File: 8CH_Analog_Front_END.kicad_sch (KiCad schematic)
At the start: 0 parts

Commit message: Routing the Digital Part
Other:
- sheet AFE_BLOCK1 renamed AFE_BLOCK_0
- sheet RFSoC_Connector_X1 ports: added B84.L1N_D01_AW5, B84.L1P_D00_AW6, B84.L2N_D03_AW3, B84.L2P_D02_AW4, B84.L3N_D05_AV2, B84.L3P_D04_AV3, B84.L4P_D06_AU2, B84.L5N_D09_AV5, B84.L5P_D08_AV6, B84.L6N_D11_AU3, B84.L6P_D10_AU4; removed none
- note added: "MUX Toggle Pin Out MUX Addr S0 Pin Out MUX Addr S1 Pin Out MUX Addr S2 Pin Out"
- note added: "RF_Swtich_Control_Pin_CH_0_CH1 RF_Swtich_Control_Pin_CH_2_CH3 RF_Swtich_Control_Pin_CH_4_CH5 RF_Swtich_Control_Pin_CH_6_CH7"
- note added: "Serial DATA Serial CLOCK Serial D_LATCH"

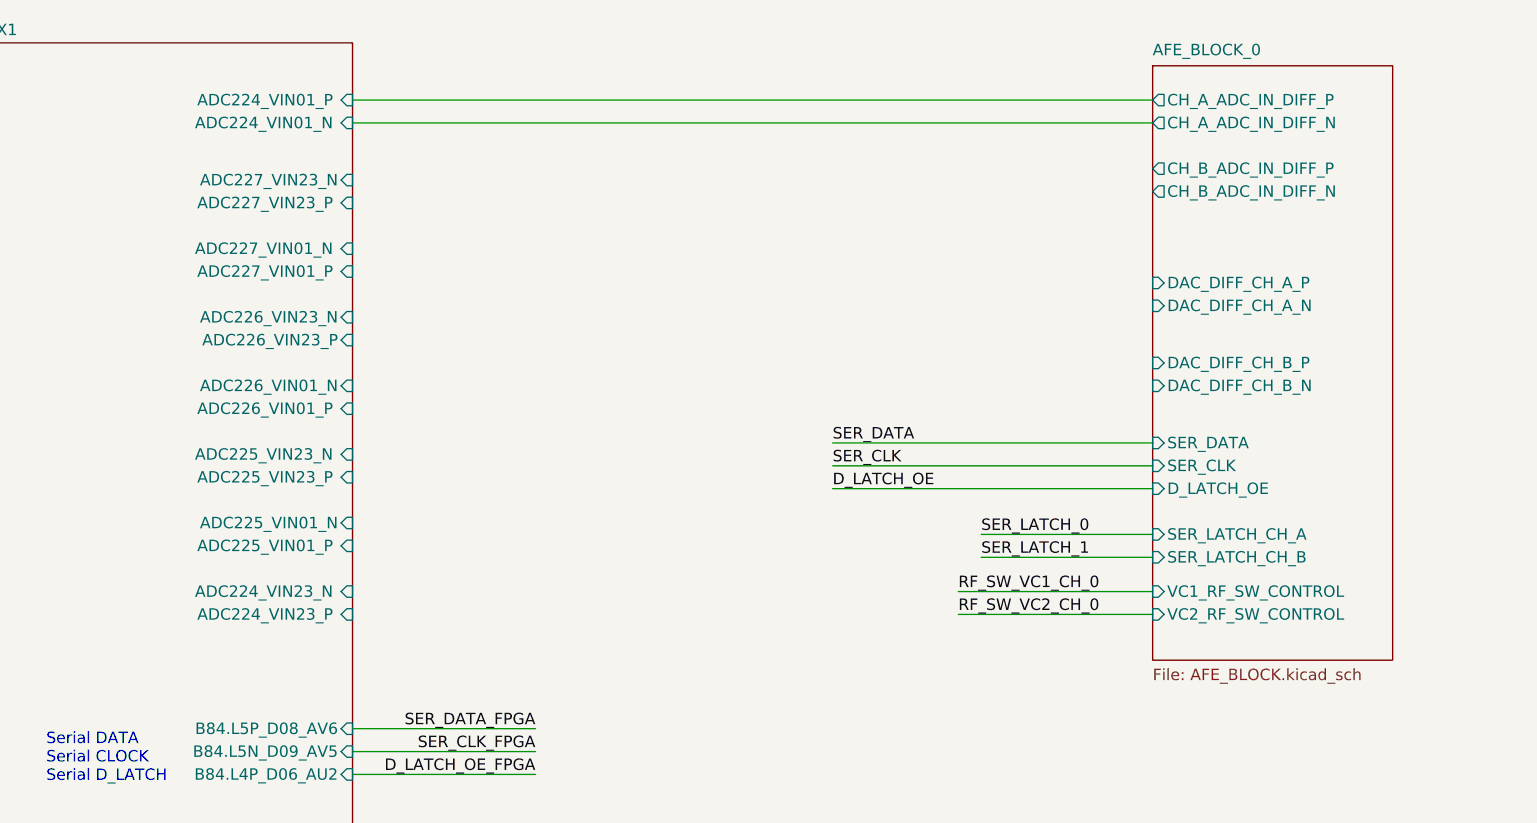
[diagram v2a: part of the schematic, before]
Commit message: Routing the Power Sector
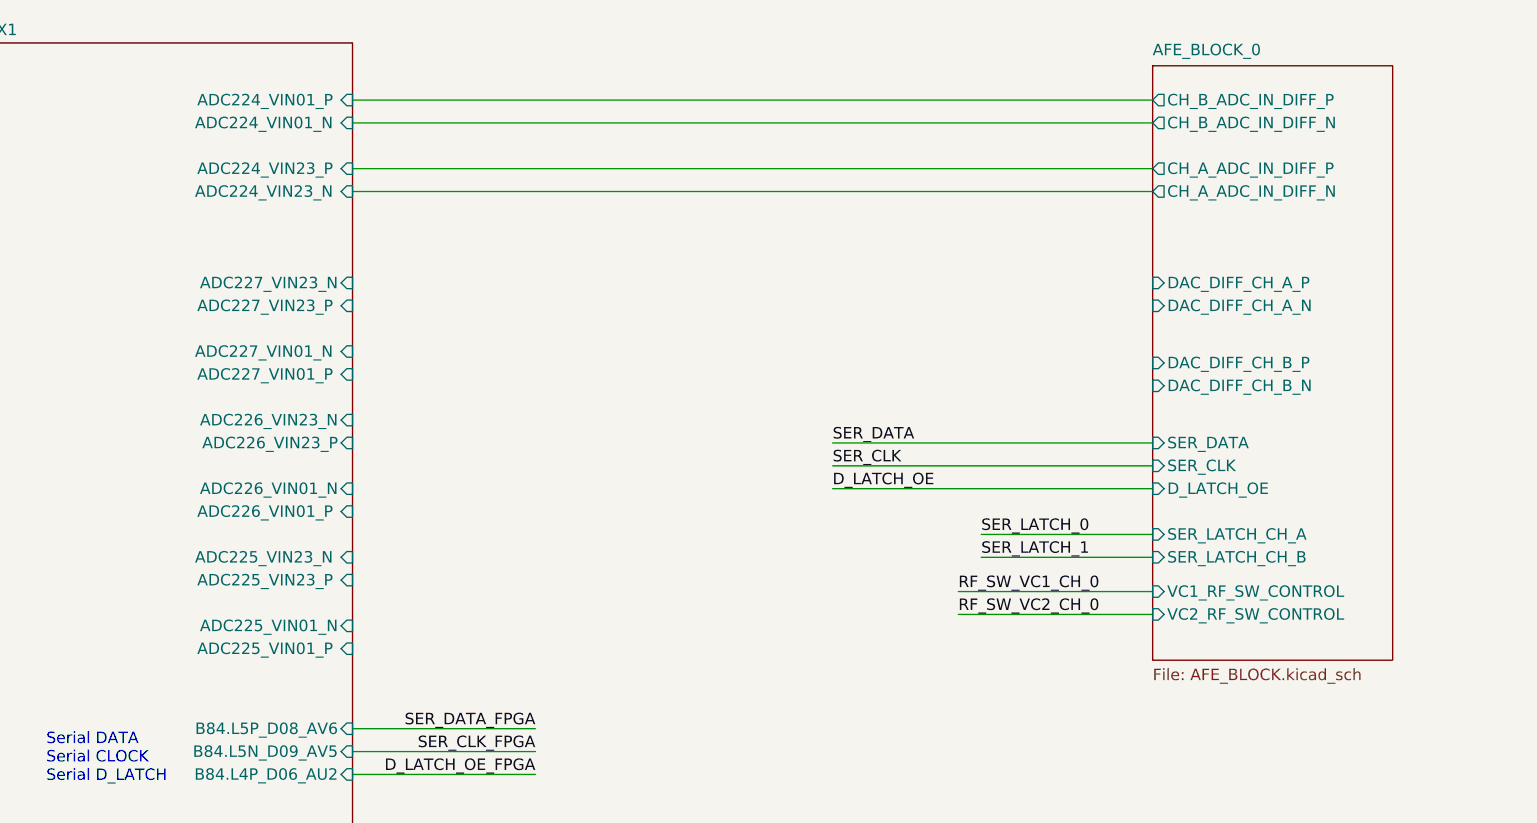
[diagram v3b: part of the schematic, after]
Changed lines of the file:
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@@
+	(wire
+		(pts
+			(xy 101.6 31.75) (xy 190.5 31.75)
+		)
+		(stroke
+			(width 0)
+			(type default)
+		)
+	)
 	(wire
 		(pts
@@
 	(wire
 		(pts
+			(xy 101.6 34.29) (xy 190.5 34.29)
+		)
+		(stroke
+			(width 0)
+			(type default)
+		)
+	)
+	(wire
+		(pts
 			(xy 149.86 124.46) (xy 170.18 124.46)
 		)
@@
 	(wire
 		(pts
-			(xy 101.6 34.29) (xy 190.5 34.29)
-		)
-		(stroke
-			(width 0)
-			(type default)
-		)
-	)
-	(wire
-		(pts
 			(xy 125.73 124.46) (xy 101.6 124.46)
 		)
@@
 	(wire
 		(pts
+			(xy 101.6 41.91) (xy 190.5 41.91)
+		)
+		(stroke
+			(width 0)
+			(type default)
+		)
+	)
+	(wire
+		(pts
 			(xy 149.86 121.92) (xy 170.18 121.92)
 		)
@@
 	(wire
 		(pts
+			(xy 101.6 39.37) (xy 190.5 39.37)
+		)
+		(stroke
+			(width 0)
+			(type default)
+		)
+	)
+	(wire
+		(pts
 			(xy 190.5 86.36) (xy 168.91 86.36)
 		)
@@
 		(pts
 			(xy 118.11 139.7) (xy 101.6 139.7)
-		)
-		(stroke
-			(width 0)
-			(type default)
-		)
-	)
-	(wire
-		(pts
-			(xy 101.6 31.75) (xy 190.5 31.75)
 		)
 		(stroke
@@
 		)
 		(pin "ADC227_VIN01_N " input
-			(at 101.6 48.26 0)
+			(at 101.6 59.69 0)
 			(effects
 				(font
@@
 		)
 		(pin "ADC227_VIN23_N" input
-			(at 101.6 40.64 0)
+			(at 101.6 52.07 0)
 			(effects
 				(font
@@
 		)
 		(pin "ADC225_VIN23_P " input
-			(at 101.6 73.66 0)
+			(at 101.6 85.09 0)
 			(effects
 				(font
@@
 		)
 		(pin "ADC224_VIN23_N " input
-			(at 101.6 86.36 0)
+			(at 101.6 41.91 0)
 			(effects
 				(font
@@
 		)
 		(pin "ADC224_VIN23_P " input
-			(at 101.6 88.9 0)
+			(at 101.6 39.37 0)
 			(effects
 				(font
@@
 		)
 		(pin "ADC225_VIN01_N" input
-			(at 101.6 78.74 0)
+			(at 101.6 90.17 0)
 			(effects
 				(font
@@
 		)
 		(pin "ADC225_VIN01_P " input
-			(at 101.6 81.28 0)
+			(at 101.6 92.71 0)
 			(effects
 				(font
@@
 		)
 		(pin "ADC226_VIN23_P" input
-			(at 101.6 58.42 0)
+			(at 101.6 69.85 0)
 			(effects
 				(font
@@
 		)
 		(pin "ADC226_VIN23_N" input
-			(at 101.6 55.88 0)
+			(at 101.6 67.31 0)
 			(effects
 				(font
@@
 		)
 		(pin "ADC227_VIN23_P " input
-			(at 101.6 43.18 0)
+			(at 101.6 54.61 0)
 			(effects
 				(font
@@
 		)
 		(pin "ADC227_VIN01_P " input
-			(at 101.6 50.8 0)
+			(at 101.6 62.23 0)
 			(effects
 				(font
@@
 		)
 		(pin "ADC226_VIN01_P " input
-			(at 101.6 66.04 0)
+			(at 101.6 77.47 0)
 			(effects
 				(font
@@
 		)
 		(pin "ADC226_VIN01_N" input
-			(at 101.6 63.5 0)
+			(at 101.6 74.93 0)
 			(effects
 				(font
@@
 		)
 		(pin "ADC225_VIN23_N " input
-			(at 101.6 71.12 0)
+			(at 101.6 82.55 0)
 			(effects
 				(font
@@
 		)
 		(pin "CH_A_ADC_IN_DIFF_N" output
-			(at 190.5 34.29 180)
+			(at 190.5 41.91 180)
 			(effects
 				(font
@@
 		)
 		(pin "CH_A_ADC_IN_DIFF_P" output
-			(at 190.5 31.75 180)
+			(at 190.5 39.37 180)
 			(effects
 				(font
@@
 		)
 		(pin "CH_B_ADC_IN_DIFF_P" output
-			(at 190.5 39.37 180)
+			(at 190.5 31.75 180)
 			(effects
 				(font
@@
 		)
 		(pin "CH_B_ADC_IN_DIFF_N" output
-			(at 190.5 41.91 180)
-			(effects
-				(font
+			(at 190.5 34.29 180)
+			(effects
+				(font

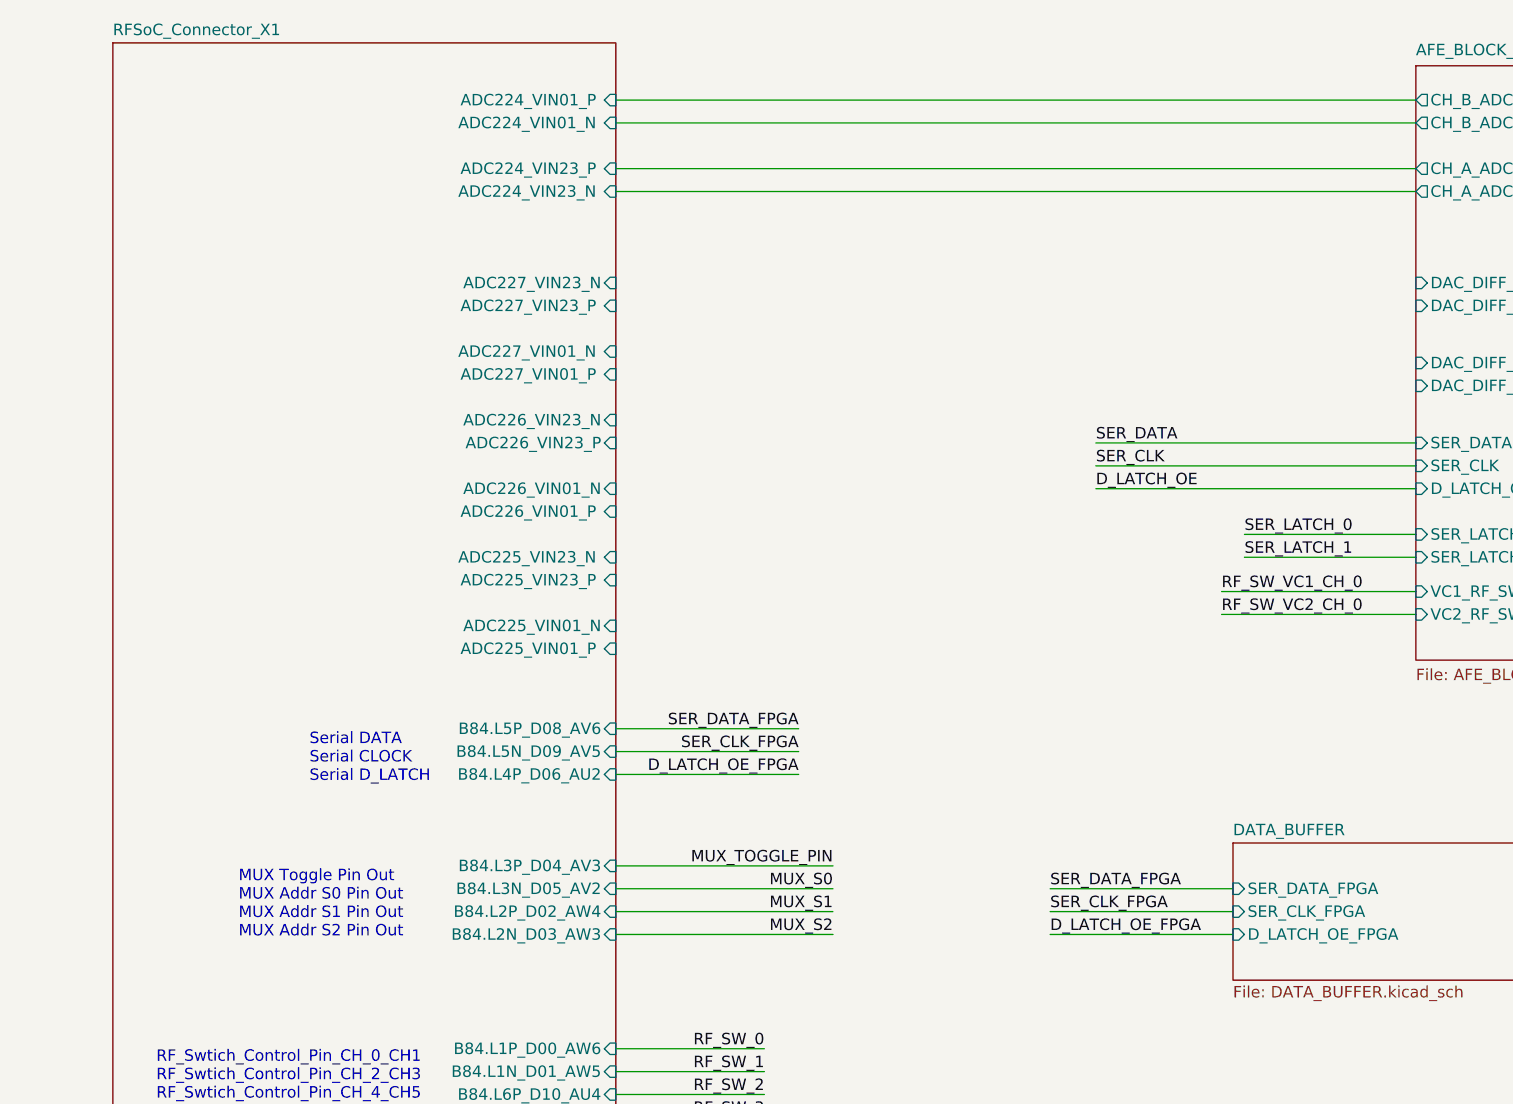
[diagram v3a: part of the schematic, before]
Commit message: Inverted the VGA output
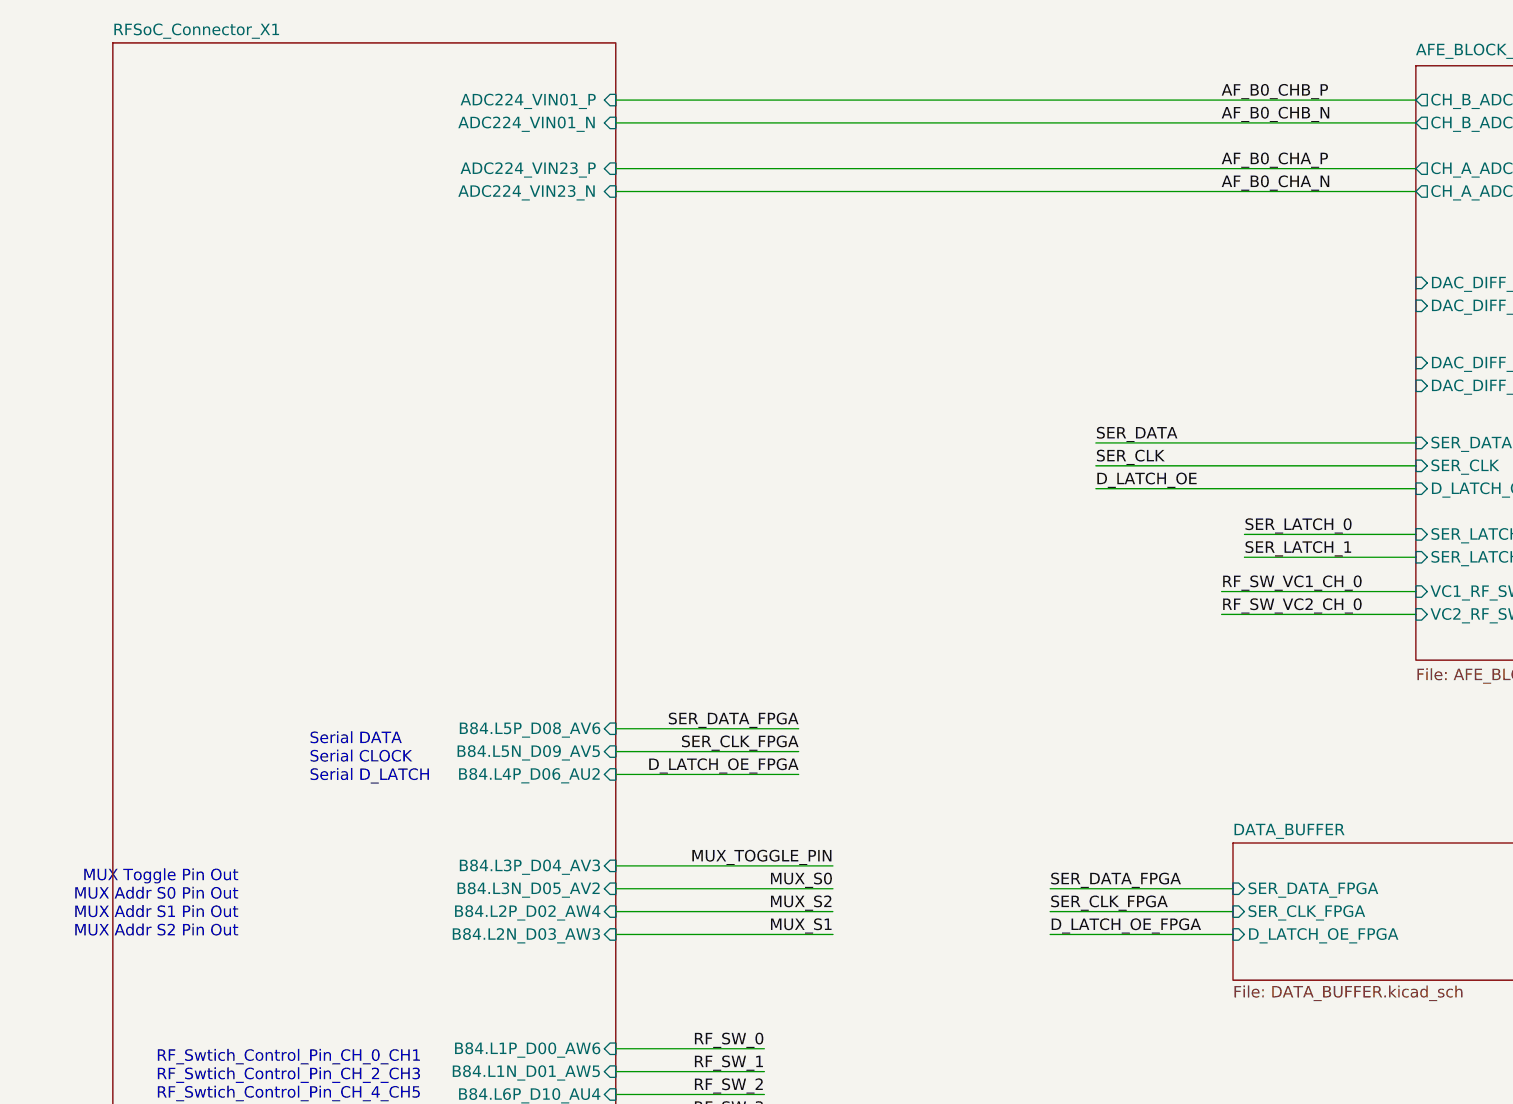
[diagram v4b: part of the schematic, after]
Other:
- sheet RFSoC_Connector_X1 ports: added none; removed ADC225_VIN01_N, ADC225_VIN01_P , ADC225_VIN23_N , ADC225_VIN23_P , ADC226_VIN01_N, ADC226_VIN01_P , ADC226_VIN23_N, ADC226_VIN23_P, ADC227_VIN01_N , ADC227_VIN01_P , ADC227_VIN23_N, ADC227_VIN23_P 

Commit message: Routing almost complete
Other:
- sheet RFSoC_Connector_X1 ports: added DAC228_VOUT0_N, DAC228_VOUT0_P, DAC229_VOUT3_N, DAC229_VOUT3_P; removed none
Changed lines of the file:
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@@
+	(wire
+		(pts
+			(xy 101.6 60.96) (xy 190.5 60.96)
+		)
+		(stroke
+			(width 0)
+			(type default)
+		)
+	)
 	(wire
 		(pts
@@
 	(wire
 		(pts
+			(xy 101.6 63.5) (xy 190.5 63.5)
+		)
+		(stroke
+			(width 0)
+			(type default)
+		)
+	)
+	(wire
+		(pts
 			(xy 256.54 119.38) (xy 220.98 119.38)
 		)
@@
 	(wire
 		(pts
+			(xy 101.6 52.07) (xy 190.5 52.07)
+		)
+		(stroke
+			(width 0)
+			(type default)
+		)
+	)
+	(wire
+		(pts
 			(xy 190.5 88.9) (xy 168.91 88.9)
 		)
@@
 		(pts
 			(xy 153.67 207.01) (xy 170.18 207.01)
+		)
+		(stroke
+			(width 0)
+			(type default)
+		)
+	)
+	(wire
+		(pts
+			(xy 101.6 54.61) (xy 190.5 54.61)
 		)
 		(stroke
@@
 			(effects
 				(font
+					(size 1.27 1.27)
+				)
+				(justify right)
+			)
+		)
+		(pin "DAC229_VOUT3_N" input
+			(at 101.6 54.61 0)
+			(effects
+				(font
+					(size 1.27 1.27)
+				)
+				(justify right)
+			)
+		)
+		(pin "DAC228_VOUT0_N" input
+			(at 101.6 63.5 0)
+			(effects
+				(font
+					(size 1.27 1.27)
+				)
+				(justify right)
+			)
+		)
+		(pin "DAC229_VOUT3_P" input
+			(at 101.6 52.07 0)
+			(effects
+				(font
+					(size 1.27 1.27)
+				)
+				(justify right)
+			)
+		)
+		(pin "DAC228_VOUT0_P" input
+			(at 101.6 60.96 0)
+			(effects
+				(font

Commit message: Routing almost complete
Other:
- sheet RFSoC_Connector_X1 ports: added DAC229_VOUT2_N, DAC229_VOUT2_P; removed none
